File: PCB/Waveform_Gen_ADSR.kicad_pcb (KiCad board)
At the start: 2 copper layers, 50.8 x 22.9 mm, 30 parts, among them J6 WAVE_OUT, M1 Feather_M4_Express, U1 AD9833, U2 LMV116, U3 AD5245, U4 AD9837, X1 ASV-25.000MHZ-E-T

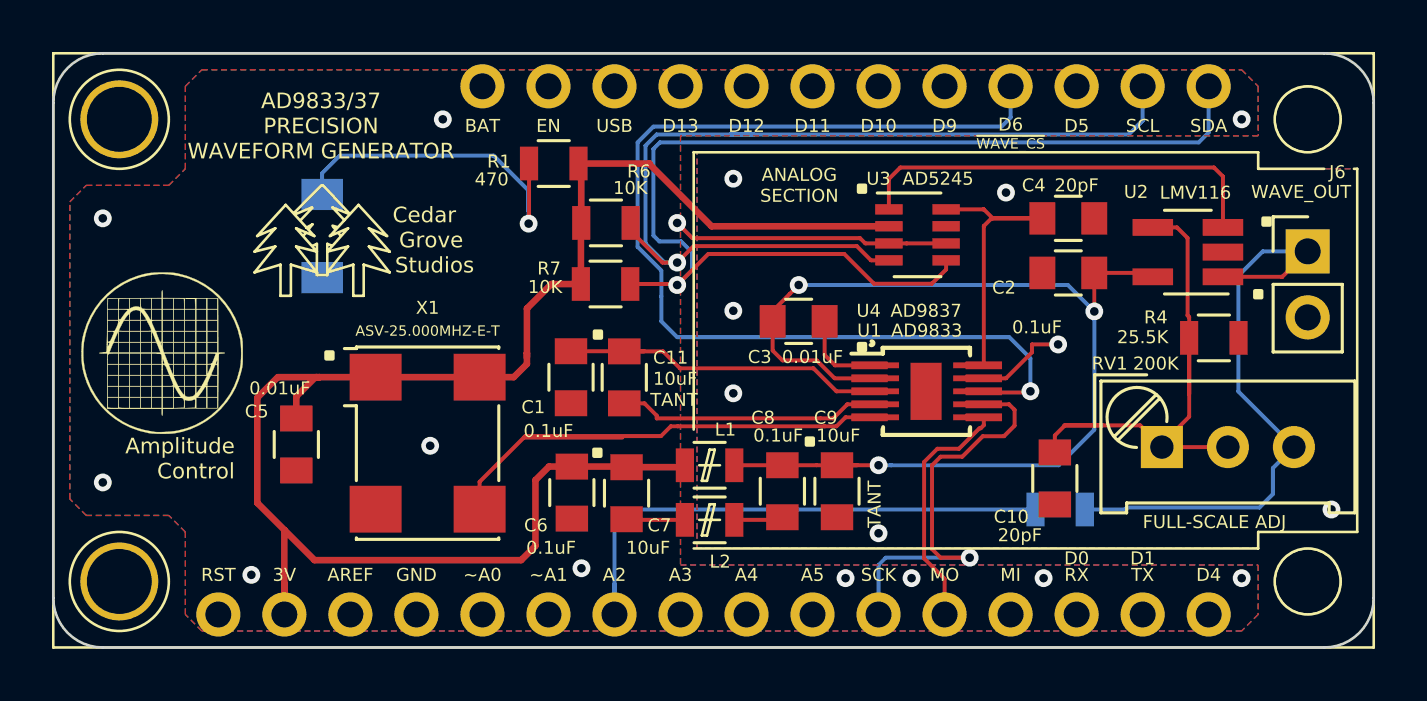
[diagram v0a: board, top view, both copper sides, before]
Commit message: change scope to support only AD9833
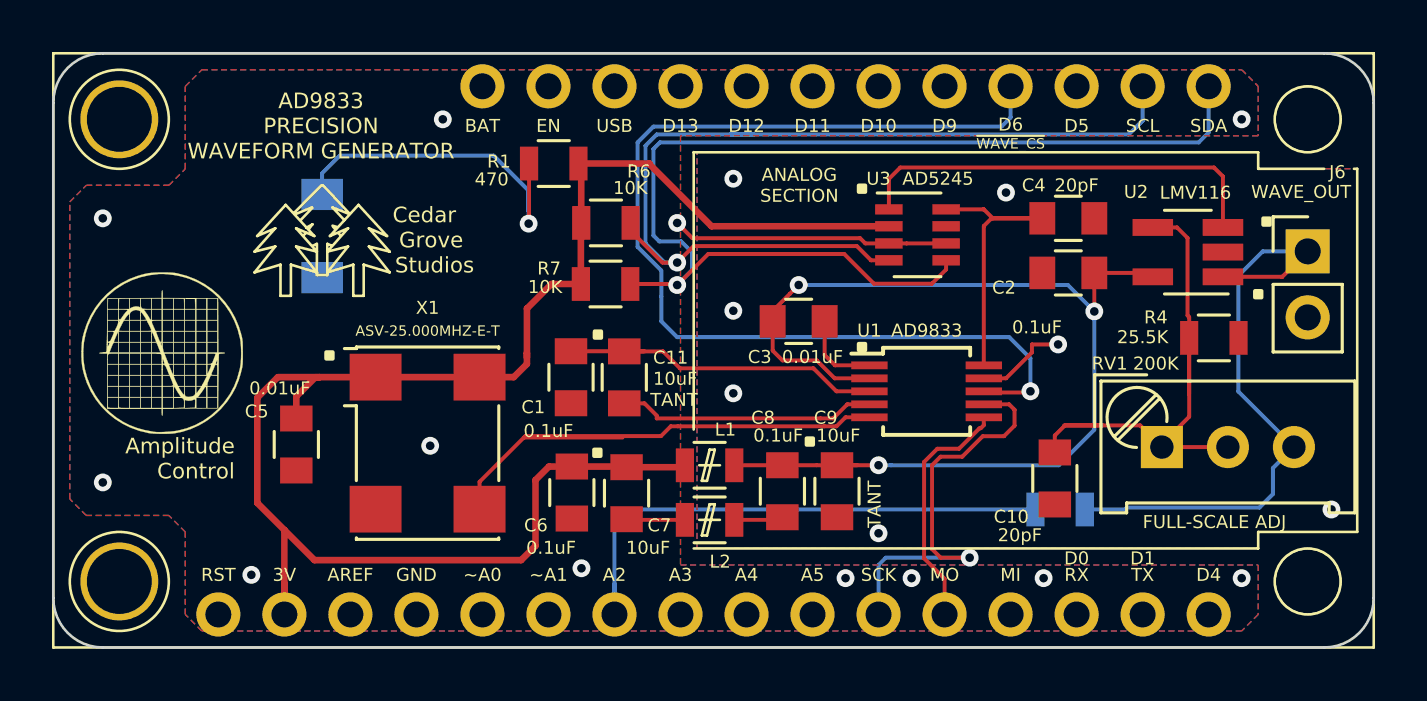
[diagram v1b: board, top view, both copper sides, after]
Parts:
- removed U4: AD9837, Housings_CSP:AD9837BCPZ-RL7
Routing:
- net /VOUT: track 12.0 -> 11.2 mm
- net /~WAVE_CS: track 41.9 -> 41.1 mm
- net GNDA: track 6.39 -> 5.62 mm
- net /SCLK: track 16.8 -> 16.0 mm
- net /MOSI: track 10.2 -> 9.38 mm
- net /COMP: track 3.92 -> 3.18 mm
- net /CAP: track 13.6 -> 12.9 mm
- net GND: track 23.6 -> 22.9 mm
- net /25MHZ_CLK: track 21.6 -> 20.9 mm
- net +3.3VA: track 43.2 -> 42.4 mm
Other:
- board text added: "2019-09-13v00"
- board text added: "AD9833 PRECISION WAVEFORM GENERATOR"
- board text added: "AD9833 Precision Waveform Generator + 8-bit amplitude control (via I2C) + FeatherWing, 3.3v powered + DC to 1MHz, 0.1Hz accuracy + Sine/Square/Triangle waveform + 3.3v buffered output + SPI interface for waveform gen (D6 = ~CS~)"
- board text removed: "2019-09-09v00"
- board text removed: "AD9833/37 PRECISION WAVEFORM GENERATOR"
- board text removed: "AD9833/37 Precision Waveform Generator + 8-bit amplitude control (via I2C) + FeatherWing, 3.3v powered + DC to 1MHz, 0.1Hz accuracy + Sine/Square/Triangle waveform + 3.3v buffered output + SPI interface for waveform gen (D6 = ~CS~)"

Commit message: update PCB layout
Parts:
- removed the G*** at (105.4, 110.0)
- removed the G*** at (99.4, 106.8) (x2)
- added G***: WAVE_GEN_LOGO, Adafruit:WAVE_GEN_LOGO, B.Cu at (105.6, 109.3)
- added G***: WAVE_GEN_LOGO, Adafruit:WAVE_GEN_LOGO, F.Cu at (99.3, 107.1)
- X1: value ASV-25.000MHZ-E-T -> 25.000MHZ
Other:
- board text added: "2019-10-19 v00"
- board text removed: "2019-09-13v00"

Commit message: update photos and board design files
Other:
- board text added: "AD9833 Precision Waveform Generator + 8-bit amplitude control (via I2C) + FeatherWing, 3.3v powered + 0.5Hz to 100kHz, 0.1Hz accuracy + Sine/Square/Triangle waveform + 3.3v buffered output + SPI interface for waveform gen (D6 = ~CS~)"
- board text removed: "AD9833 Precision Waveform Generator + 8-bit amplitude control (via I2C) + FeatherWing, 3.3v powered + DC to 1MHz, 0.1Hz accuracy + Sine/Square/Triangle waveform + 3.3v buffered output + SPI interface for waveform gen (D6 = ~CS~)"
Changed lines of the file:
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@@
     (effects (font (size 0.8 0.8) (thickness 0.16)) (justify right mirror))
   )
-  (gr_text "AD9833 Precision Waveform Generator\n  + 8-bit amplitude control (via I2C)\n  + FeatherWing, 3.3v powered\n  + DC to 1MHz, 0.1Hz accuracy\n  + Sine/Square/Triangle waveform\n  + 3.3v buffered output\n  + SPI interface for waveform gen (D6 = ~CS~)" (at 142.53 104.11) (layer B.SilkS)
+  (gr_text "AD9833 Precision Waveform Generator\n  + 8-bit amplitude control (via I2C)\n  + FeatherWing, 3.3v powered\n  + 0.5Hz to 100kHz, 0.1Hz accuracy\n  + Sine/Square/Triangle waveform\n  + 3.3v buffered output\n  + SPI interface for waveform gen (D6 = ~CS~)" (at 142.53 104.11) (layer B.SilkS)
     (effects (font (size 0.6 0.6) (thickness 0.12)) (justify left mirror))
   )

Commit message: update backup folder
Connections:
- net /~WAVE_CS renamed /~{WAVE_CS}
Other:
- net class Default removed
- net class Power removed
- board text added: "AD9833 Precision Waveform Generator + 8-bit amplitude control (via I2C) + FeatherWing, 3.3v powered + 0.5Hz to 100kHz, 0.1Hz accuracy + Sine/Square/Triangle waveform + 3.3v buffered output + SPI interface for waveform gen (D6 = ~{CS})"
- board text added: "~{WAVE_CS}"
- board text removed: "AD9833 Precision Waveform Generator + 8-bit amplitude control (via I2C) + FeatherWing, 3.3v powered + 0.5Hz to 100kHz, 0.1Hz accuracy + Sine/Square/Triangle waveform + 3.3v buffered output + SPI interface for waveform gen (D6 = ~CS~)"
- board text removed: "~WAVE_CS"
